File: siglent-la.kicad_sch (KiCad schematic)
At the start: 1 part, among them J1 Bus_PCI_Express_x1

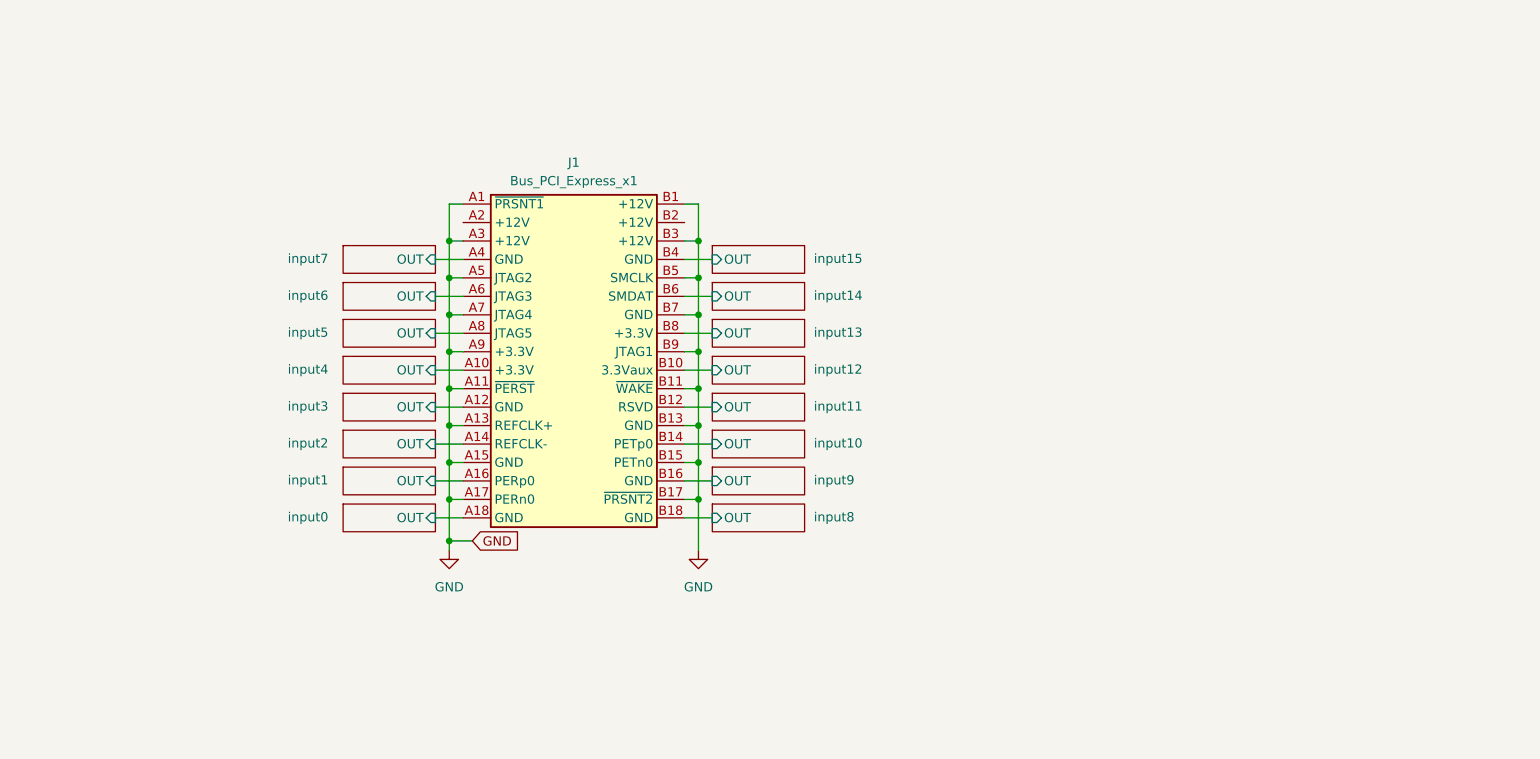
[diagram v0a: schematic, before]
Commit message: ufl connector
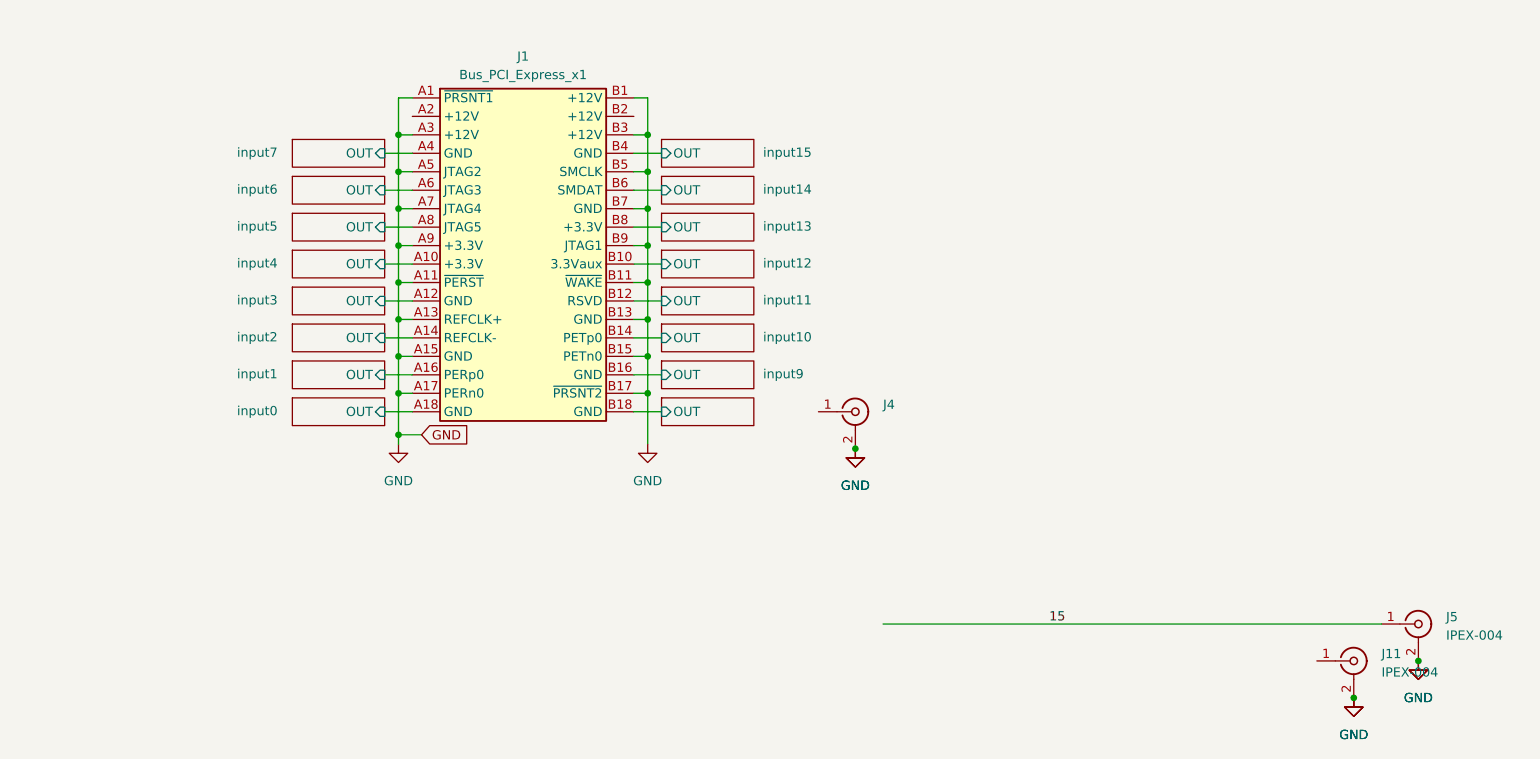
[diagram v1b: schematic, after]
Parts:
- added J11, J5: IPEX-004, Connector_Coaxial:SMA_Amphenol_132289_EdgeMount, symbol Connector:Conn_Coaxial
- added J4: IPEX-004, Connector_Coaxial:U.FL_Molex_MCRF_73412-0110_Vertical, symbol Connector:Conn_Coaxial
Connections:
- net GND: now also J11.2 (Ext), J4.2 (Ext), J5.2 (Ext)
- new net 15: J5.1 (In)
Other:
- moved on the sheet: J1

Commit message: rj45 version of the logic analyzer
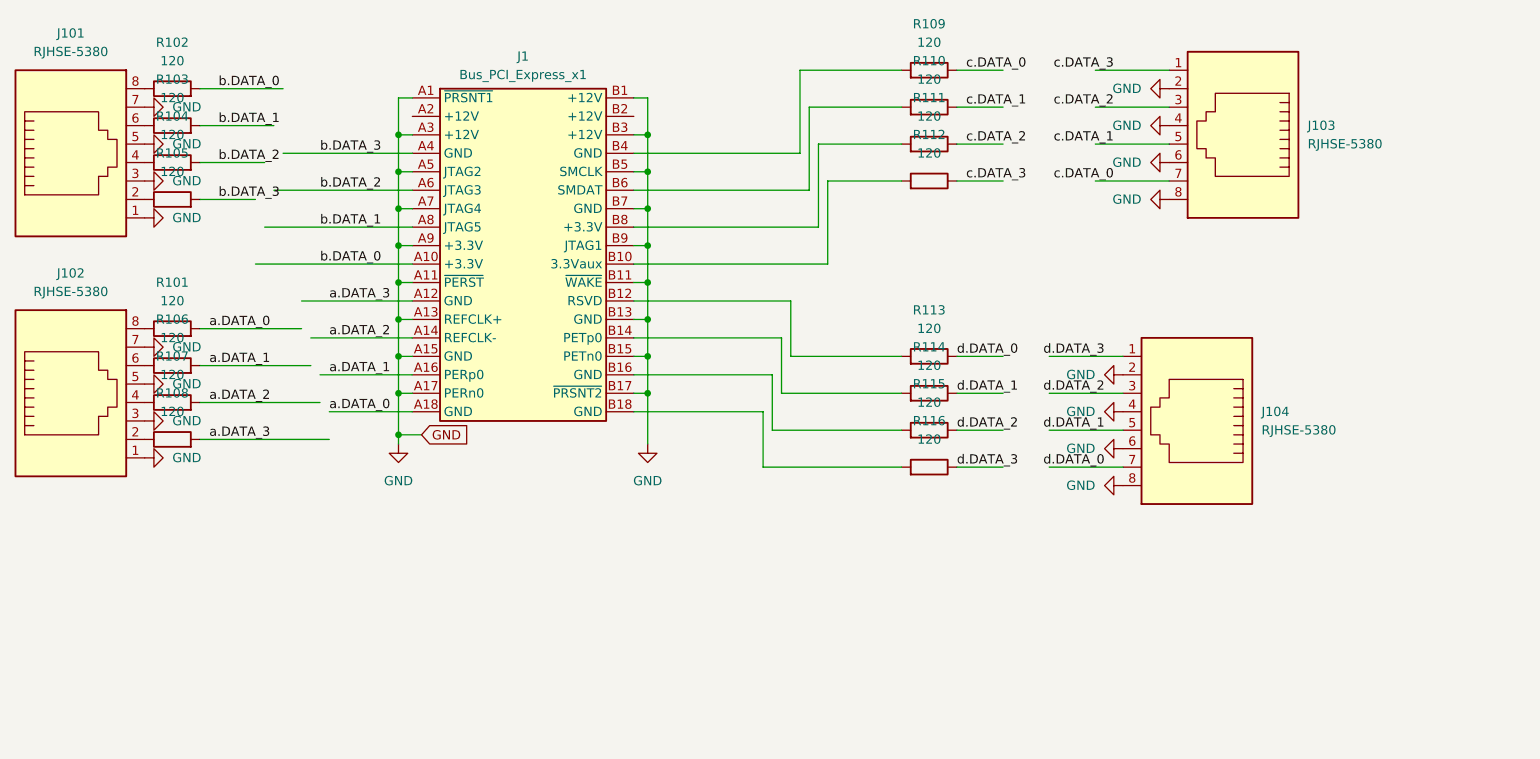
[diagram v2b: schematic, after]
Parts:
- removed J11, J5: IPEX-004, Connector_Coaxial:SMA_Amphenol_132289_EdgeMount, symbol Connector:Conn_Coaxial
- removed J4: IPEX-004, Connector_Coaxial:U.FL_Molex_MCRF_73412-0110_Vertical, symbol Connector:Conn_Coaxial
- added J101, J102, J103, J104: RJHSE-5380, Connector_RJ:RJ45_OST_PJ012-8P8CX_Vertical, symbol Connector:RJ45
- added R101, R102, R103, R104, R105, R106, R107, R108, R109, R110, R111, R112, R113, R114, R115, R116: 120, Resistor_SMD:R_0603_1608Metric, symbol Device:R
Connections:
- net GND: now also J101.1, J101.3, J101.5, J101.7, J102.1, J102.3, J102.5, J102.7, J103.2, J103.4, J103.6, J103.8, J104.2, J104.4, J104.6, J104.8
- net input0/OUT renamed a.DATA_0
- net a.DATA_0: now also R101.2
- net input1/OUT renamed a.DATA_1
- net a.DATA_1: now also R106.2
- net input10/OUT: no longer names the net of J1.B14 (PETp0)
- net input10/OUT: now also R114.2
- net input11/OUT: no longer names the net of J1.B12 (RSVD)
- net input11/OUT: now also R113.2
- net input12/OUT: no longer names the net of J1.B10 (3.3Vaux)
- net input12/OUT: now also R112.2
- net input13/OUT: no longer names the net of J1.B8 (+3.3V)
- net input13/OUT: now also R111.2
- net input14/OUT: no longer names the net of J1.B6 (SMDAT)
- net input14/OUT: now also R110.2
- net input15/OUT: no longer names the net of J1.B4 (GND)
- net input15/OUT: now also R109.2
- net input2/OUT renamed a.DATA_2
- net a.DATA_2: now also R107.2
- net input3/OUT renamed a.DATA_3
- net a.DATA_3: now also R108.2
- net input4/OUT renamed b.DATA_0
- net b.DATA_0: now also R102.2
- net input5/OUT renamed b.DATA_1
- net b.DATA_1: now also R103.2
- net input6/OUT renamed b.DATA_2
- net b.DATA_2: now also R104.2
- net input7/OUT renamed b.DATA_3
- net b.DATA_3: now also R105.2
- net input8/OUT: no longer names the net of J1.B18 (GND)
- net input8/OUT: now also R116.2
- net input9/OUT: no longer names the net of J1.B16 (GND)
- net input9/OUT: now also R115.2
- new net: J102.2, R108.1
- new net: J101.2, R105.1
- new net: J101.4, R104.1
- new net: J101.6, R103.1
- new net: J101.8, R102.1
- new net: J102.8, R101.1
- new net: J102.6, R106.1
- new net: J102.4, R107.1
- new net c.DATA_0: J103.7, R109.1
- new net c.DATA_1: J103.5, R110.1
- new net c.DATA_2: J103.3, R111.1
- new net c.DATA_3: J103.1, R112.1
- new net d.DATA_0: J104.7, R113.1
- new net d.DATA_1: J104.5, R114.1
- new net d.DATA_2: J104.3, R115.1
- new net d.DATA_3: J104.1, R116.1
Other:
- removed sheet input0
- removed sheet input1
- removed sheet input10
- removed sheet input11
- removed sheet input12
- removed sheet input13
- removed sheet input14
- removed sheet input15
- removed sheet input2
- removed sheet input3
- removed sheet input4
- removed sheet input5
- removed sheet input6
- removed sheet input7
- removed sheet input8
- removed sheet input9
